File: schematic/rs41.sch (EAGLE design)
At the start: 268 parts, among them J201 SENSORBOOM, J601 expansion, J602 XDATA, Q201 BSS92, Q202 BSS92, Q203 BSS101, Q204 BSS101, Q501 BSS92, Q502 BSS101, Q503 BSS101, Q601 BSS101, U101 STM32F100C8T6B, U201 TS3A4751, U202 TS5A9411, U203 TS5A9411, U204 TS5A9411, U205 74HCU04, U206 305G, U207 74LVC3G34, U208 NC7SZ27, U301 DIFFGEN, U302 UBX-6010MLF56, U303 SAW, U304 LNA, U401 SI4032QFN204X4, U501 TLV70030SOT23-5, U502 TPS61200, U503 TLV70030SOT23-5, U504 TLV70030SOT23-5, U601 25AA080SN, X101 24MHz, X301 OSC_GPSXTAL4

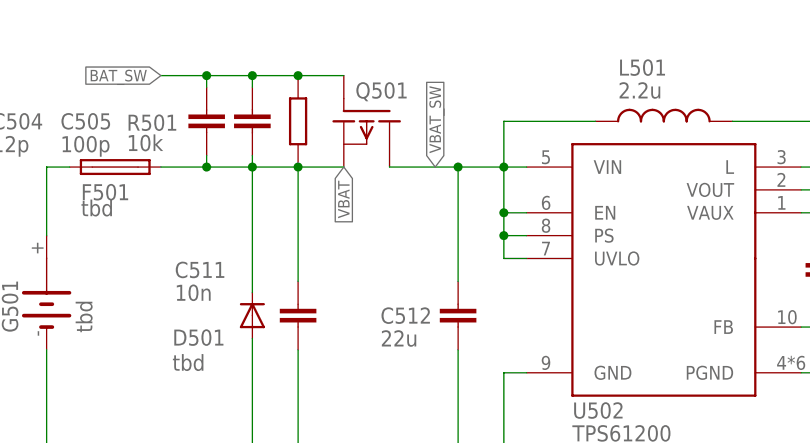
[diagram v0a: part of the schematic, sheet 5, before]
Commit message: Q501: added note and corected footprint
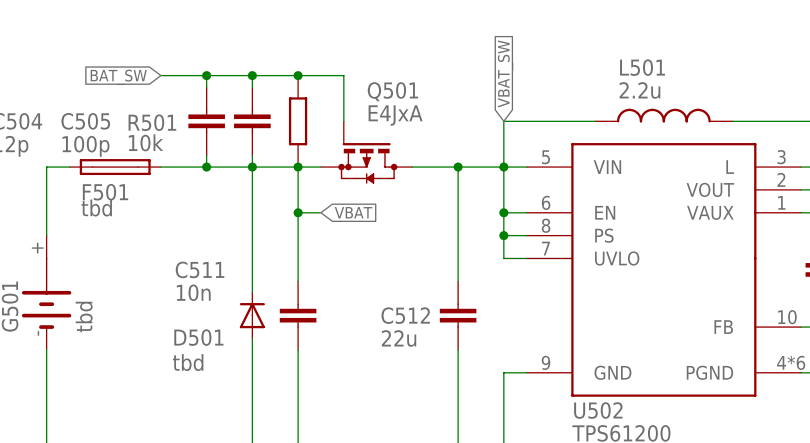
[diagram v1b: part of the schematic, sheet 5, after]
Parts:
- Q501: value BSS92 -> E4JxA; device transistor-fet:BSS92 -> transistor-small-signal:BSS84

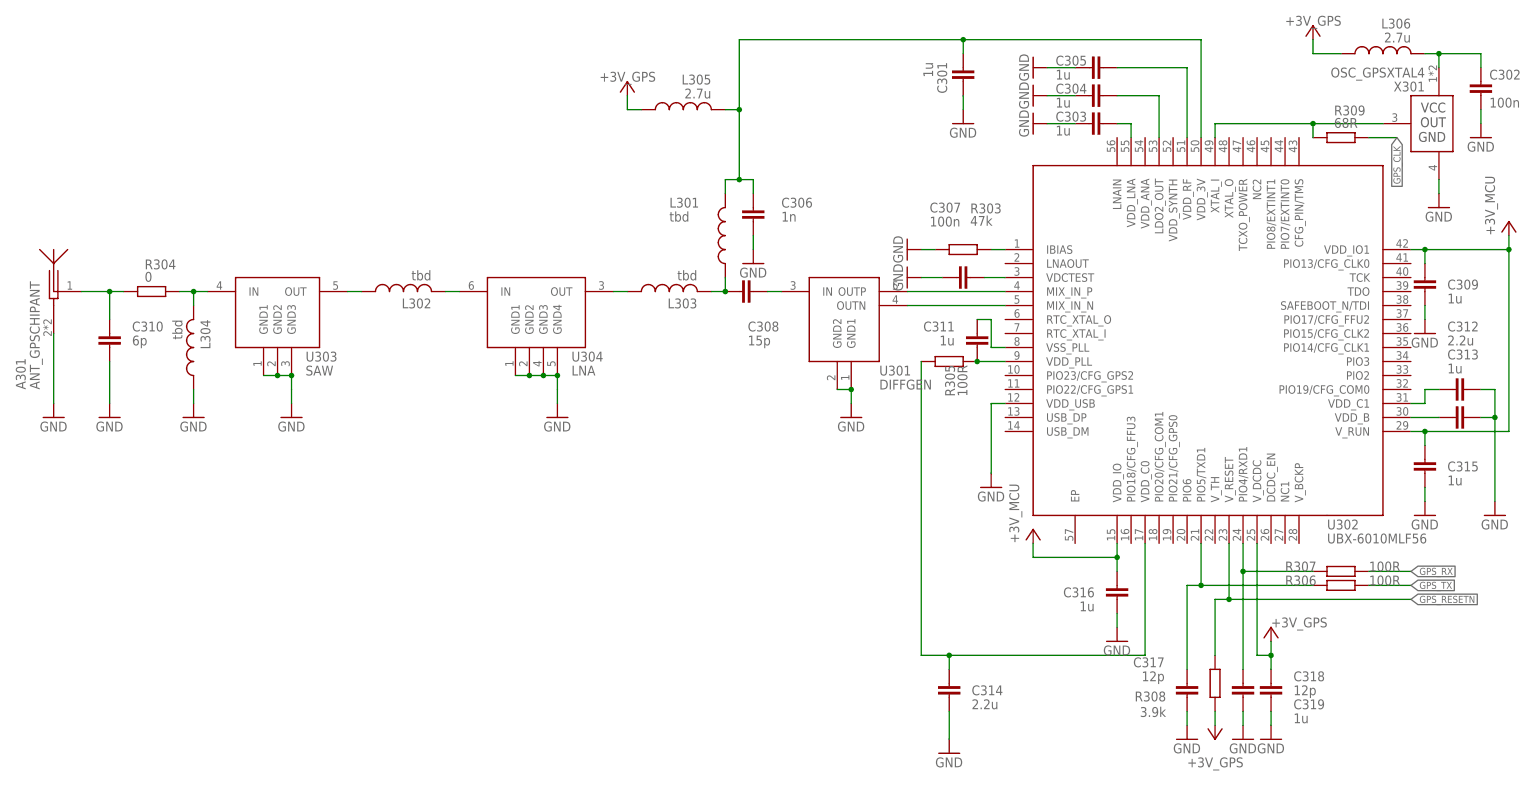
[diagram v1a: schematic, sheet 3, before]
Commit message: sorted GPS sheet
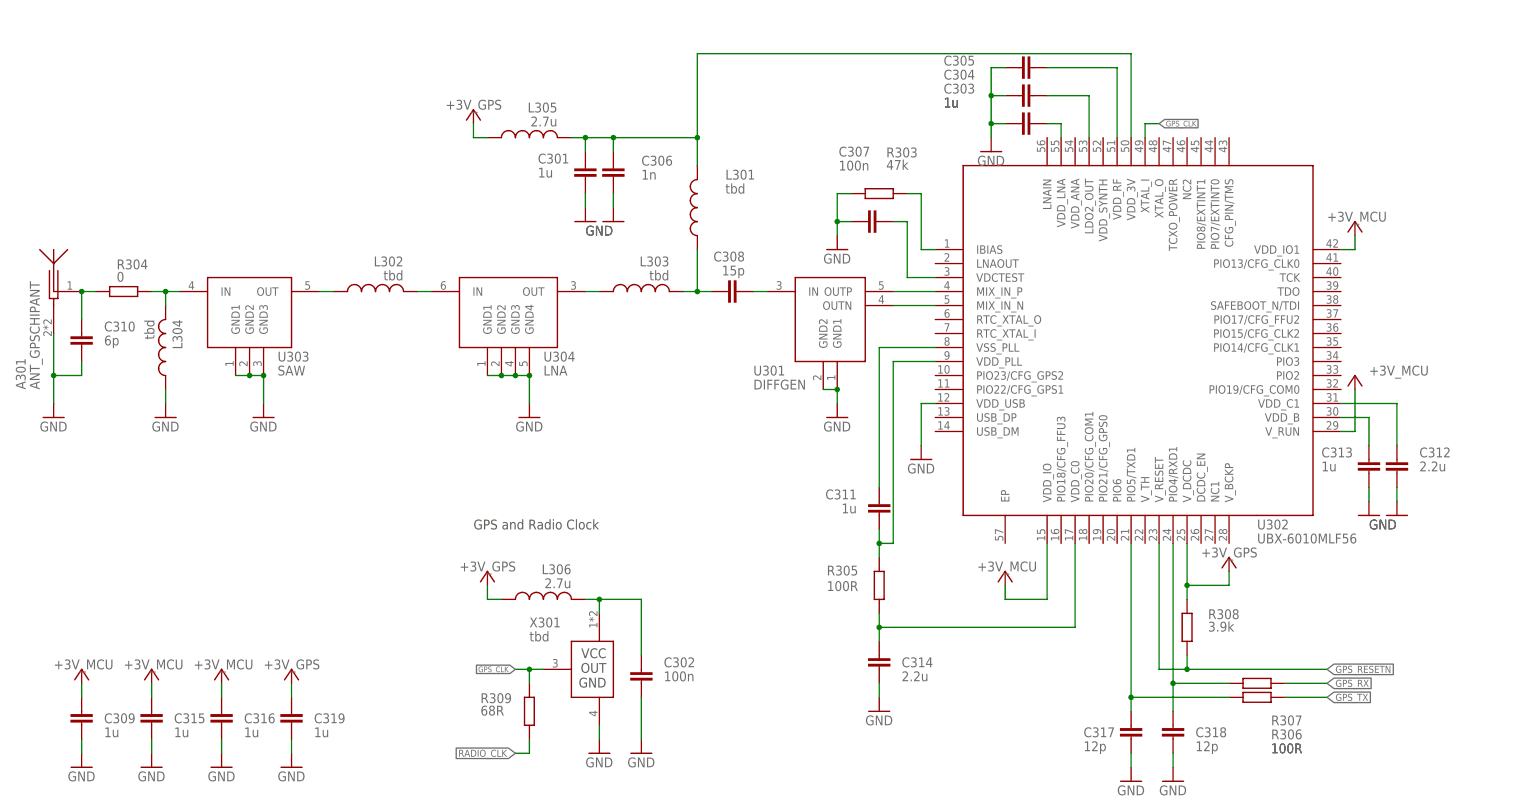
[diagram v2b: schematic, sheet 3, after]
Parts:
- X301: value OSC_GPSXTAL4 -> tbd
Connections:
- removed net N$65: R309.2, U302.XTAL_I, X301.OUT
- new net RADIO_CLK: C401.2, R309.1
- net +3V_GPS: now also R308.1; no longer R308.2
- net +3V_MCU: now also C316.1; no longer C316.2
- net GND: now also C316.2; no longer C316.1
- net GPS_CLK: now also R309.2, U302.XTAL_I, X301.OUT; no longer C401.2, R309.1
- net GPS_RESETN: now also R308.2; no longer R308.1
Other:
- note added: "GPS and Radio Clock"
- note added: "GSD pinout, reverse Diode, U_DSON = 0.65V, U_SD = 0.91V"
- moved on the sheet: C301, C302, C303, C304, C305, C306, C307, C308, C309, C310, C311, C312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

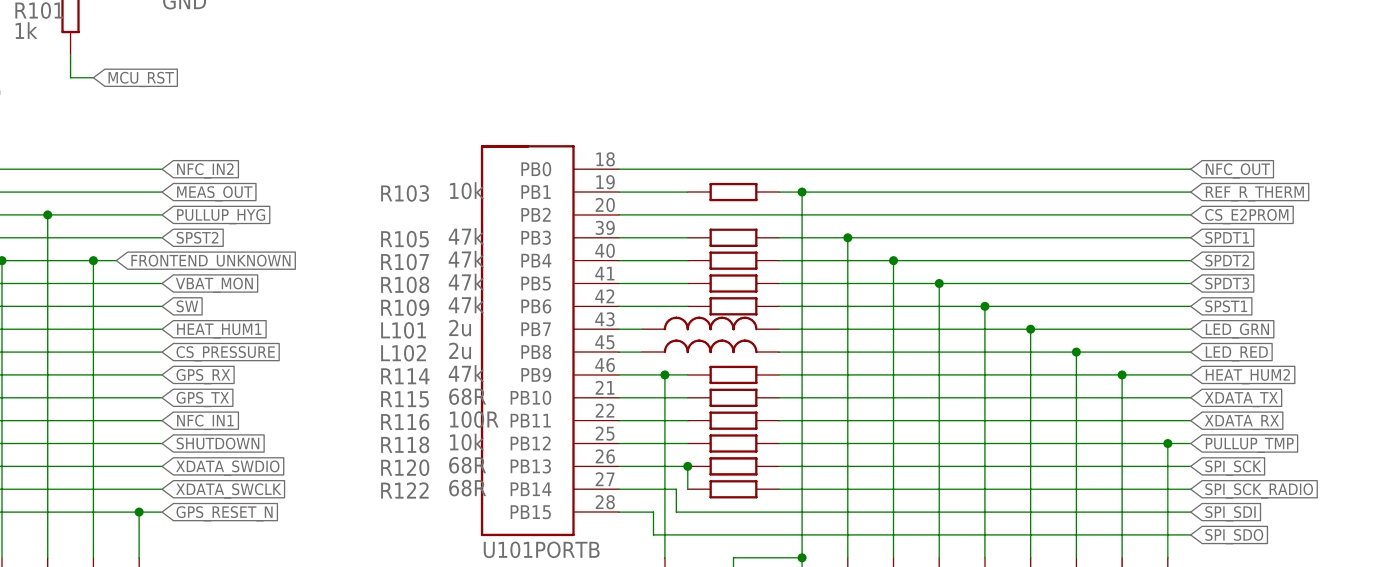
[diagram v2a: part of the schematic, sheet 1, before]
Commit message: renamed CS Signals
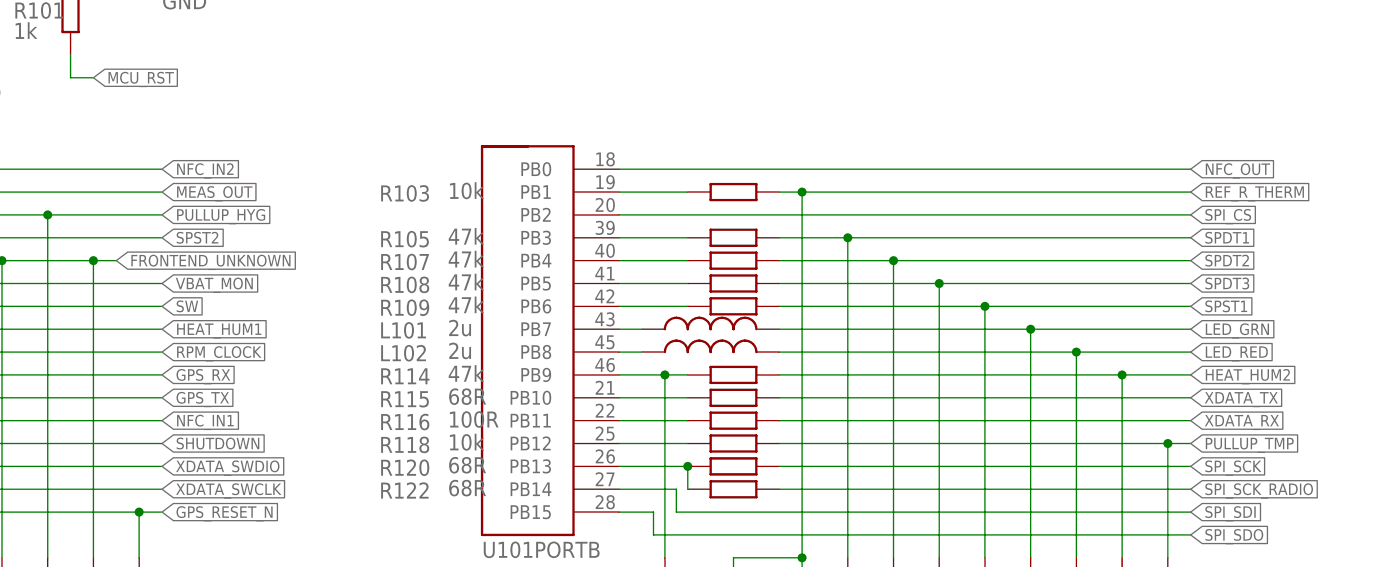
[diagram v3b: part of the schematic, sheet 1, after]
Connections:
- net CS_E2PROM renamed SPI_CS
- new net RPM_CLOCK: R112.1
- net CS_PRESSURE: no longer R112.1
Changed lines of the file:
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@@
 <grid distance="0.1" unitdist="inch" unit="inch" style="lines" multiple="1" display="no" altdistance="0.01" altunitdist="inch" altunit="inch"/>
 <layers>
-<layer number="1" name="Top" color="4" fill="1" visible="yes" active="no"/>
-<layer number="2" name="Route2" color="1" fill="3" visible="yes" active="no"/>
-<layer number="3" name="Route3" color="4" fill="3" visible="yes" active="no"/>
-<layer number="4" name="Route4" color="1" fill="4" visible="yes" active="no"/>
-<layer number="5" name="Route5" color="4" fill="4" visible="yes" active="no"/>
-<layer number="6" name="Route6" color="1" fill="8" visible="yes" active="no"/>
-<layer number="7" name="Route7" color="4" fill="8" visible="yes" active="no"/>
-<layer number="8" name="Route8" color="1" fill="2" visible="yes" active="no"/>
-<layer number="9" name="Route9" color="4" fill="2" visible="yes" active="no"/>
-<layer number="10" name="Route10" color="1" fill="7" visible="yes" active="no"/>
-<layer number="11" name="Route11" color="4" fill="7" visible="yes" active="no"/>
-<layer number="12" name="Route12" color="1" fill="5" visible="yes" active="no"/>
-<layer number="13" name="Route13" color="4" fill="5" visible="yes" active="no"/>
-<layer number="14" name="Route14" color="1" fill="6" visible="yes" active="no"/>
-<layer number="15" name="Route15" color="4" fill="6" visible="yes" active="no"/>
-<layer number="16" name="Bottom" color="1" fill="1" visible="yes" active="no"/>
-<layer number="17" name="Pads" color="2" fill="1" visible="yes" active="no"/>
-<layer number="18" name="Vias" color="2" fill="1" visible="yes" active="no"/>
-<layer number="19" name="Unrouted" color="6" fill="1" visible="yes" active="no"/>
-<layer number="20" name="Dimension" color="24" fill="1" visible="yes" active="no"/>
-<layer number="21" name="tPlace" color="7" fill="1" visible="yes" active="no"/>
-<layer number="22" name="bPlace" color="7" fill="1" visible="yes" active="no"/>
-<layer number="23" name="tOrigins" color="15" fill="1" visible="yes" active="no"/>
-<layer number="24" name="bOrigins" color="15" fill="1" visible="yes" active="no"/>
-<layer number="25" name="tNames" color="7" fill="1" visible="yes" active="no"/>
-<layer number="26" name="bNames" color="7" fill="1" visible="yes" active="no"/>
-<layer number="27" name="tValues" color="7" fill="1" visible="yes" active="no"/>
-<layer number="28" name="bValues" color="7" fill="1" visible="yes" active="no"/>
+<layer number="1" name="Top" color="4" fill="1" visible="no" active="no"/>
+<layer number="2" name="Route2" color="1" fill="3" visible="no" active="no"/>
+<layer number="3" name="Route3" color="4" fill="3" visible="no" active="no"/>
+<layer number="4" name="Route4" color="1" fill="4" visible="no" active="no"/>
+<layer number="5" name="Route5" color="4" fill="4" visible="no" active="no"/>
+<layer number="6" name="Route6" color="1" fill="8" visible="no" active="no"/>
+<layer number="7" name="Route7" color="4" fill="8" visible="no" active="no"/>
+<layer number="8" name="Route8" color="1" fill="2" visible="no" active="no"/>
+<layer number="9" name="Route9" color="4" fill="2" visible="no" active="no"/>
+<layer number="10" name="Route10" color="1" fill="7" visible="no" active="no"/>
+<layer number="11" name="Route11" color="4" fill="7" visible="no" active="no"/>
+<layer number="12" name="Route12" color="1" fill="5" visible="no" active="no"/>
+<layer number="13" name="Route13" color="4" fill="5" visible="no" active="no"/>
+<layer number="14" name="Route14" color="1" fill="6" visible="no" active="no"/>
+<layer number="15" name="Route15" color="4" fill="6" visible="no" active="no"/>
+<layer number="16" name="Bottom" color="1" fill="1" visible="no" active="no"/>
+<layer number="17" name="Pads" color="2" fill="1" visible="no" active="no"/>
+<layer number="18" name="Vias" color="2" fill="1" visible="no" active="no"/>
+<layer number="19" name="Unrouted" color="6" fill="1" visible="no" active="no"/>
+<layer number="20" name="Dimension" color="24" fill="1" visible="no" active="no"/>
+<layer number="21" name="tPlace" color="7" fill="1" visible="no" active="no"/>
+<layer number="22" name="bPlace" color="7" fill="1" visible="no" active="no"/>
+<layer number="23" name="tOrigins" color="15" fill="1" visible="no" active="no"/>
+<layer number="24" name="bOrigins" color="15" fill="1" visible="no" active="no"/>
+<layer number="25" name="tNames" color="7" fill="1" visible="no" active="no"/>
+<layer number="26" name="bNames" color="7" fill="1" visible="no" active="no"/>
+<layer number="27" name="tValues" color="7" fill="1" visible="no" active="no"/>
+<layer number="28" name="bValues" color="7" fill="1" visible="no" active="no"/>
 <layer number="29" name="tStop" color="7" fill="3" visible="no" active="no"/>
 <layer number="30" name="bStop" color="7" fill="6" visible="no" active="no"/>
@@
 <layer number="35" name="tGlue" color="7" fill="4" visible="no" active="no"/>
 <layer number="36" name="bGlue" color="7" fill="5" visible="no" active="no"/>
-<layer number="37" name="tTest" color="7" fill="1" visible="yes" active="no"/>
-<layer number="38" name="bTest" color="7" fill="1" visible="yes" active="no"/>
+<layer number="37" name="tTest" color="7" fill="1" visible="no" active="no"/>
+<layer number="38" name="bTest" color="7" fill="1" visible="no" active="no"/>
 <layer number="39" name="tKeepout" color="4" fill="11" visible="no" active="no"/>
 <layer number="40" name="bKeepout" color="1" fill="11" visible="no" active="no"/>
@@
 <layer number="44" name="Drills" color="7" fill="1" visible="no" active="no"/>
 <layer number="45" name="Holes" color="7" fill="1" visible="no" active="no"/>
-<layer number="46" name="Milling" color="3" fill="1" visible="yes" active="no"/>
-<layer number="47" name="Measures" color="7" fill="1" visible="yes" active="no"/>
-<layer number="48" name="Document" color="7" fill="1" visible="yes" active="no"/>
-<layer number="49" name="Reference" color="7" fill="1" visible="yes" active="no"/>
-<layer number="50" name="dxf" color="7" fill="1" visible="yes" active="no"/>
-<layer number="51" name="tDocu" color="7" fill="1" visible="yes" active="no"/>
-<layer number="52" name="bDocu" color="7" fill="1" visible="yes" active="no"/>
-<layer number="53" name="tPadExt" color="7" fill="1" visible="yes" active="no"/>
-<layer number="54" name="bPadExt" color="1" fill="1" visible="yes" active="no"/>
+<layer number="46" name="Milling" color="3" fill="1" visible="no" active="no"/>
+<layer number="47" name="Measures" color="7" fill="1" visible="no" active="no"/>
+<layer number="48" name="Document" color="7" fill="1" visible="no" active="no"/>
+<layer number="49" name="Reference" color="7" fill="1" visible="no" active="no"/>
+<layer number="50" name="dxf" color="7" fill="1" visible="no" active="no"/>
+<layer number="51" name="tDocu" color="7" fill="1" visible="no" active="no"/>
+<layer number="52" name="bDocu" color="7" fill="1" visible="no" active="no"/>
+<layer number="53" name="tPadExt" color="7" fill="1" visible="no" active="no"/>
+<layer number="54" name="bPadExt" color="1" fill="1" visible="no" active="no"/>
 <layer number="88" name="SimResults" color="9" fill="1" visible="yes" active="yes"/>
 <layer number="89" name="SimProbes" color="9" fill="1" visible="yes" active="yes"/>
@@
 </segment>
 </net>
-<net name="CS_PRESSURE" class="0">
-<segment>
-<pinref part="R112" gate="G$1" pin="1"/>
-<wire x1="2.54" y1="22.86" x2="-17.78" y2="22.86" width="0.1524" layer="91"/>
-<label x="2.54" y="22.86" size="1.27" layer="95" xref="yes"/>
-</segment>
-</net>
 <net name="HEAT_HUM1" class="0">
 <segment>
@@
 </segment>
 </net>
-<net name="CS_E2PROM" class="0">
+<net name="SPI_CS" class="0">
 <segment>
 <pinref part="U101" gate="PORTB" pin="PB2"/>
@@
 </segment>
 </net>
+<net name="RPM_CLOCK" class="0">
+<segment>
+<pinref part="R112" gate="G$1" pin="1"/>
+<wire x1="2.54" y1="22.86" x2="-17.78" y2="22.86" width="0.1524" layer="91"/>
+<label x="2.54" y="22.86" size="1.27" layer="95" xref="yes"/>
+</segment>
+</net>
 </nets>
 </sheet>
@@
 </segment>
 </net>
-<net name="CS_E2PROM" class="0">
+<net name="SPI_CS" class="0">
 <segment>
 <pinref part="J601" gate="G$1" pin="12"/>
